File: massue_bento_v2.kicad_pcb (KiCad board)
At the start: 2 copper layers, 100 x 21 mm, 69 parts, among them K1 CONN_3, K2 CONN_3, K3 CONN_3, P1 TST, P10 CONN_1, P11 TST, P12 TST, P13 TST, P14 TST, P15 TST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

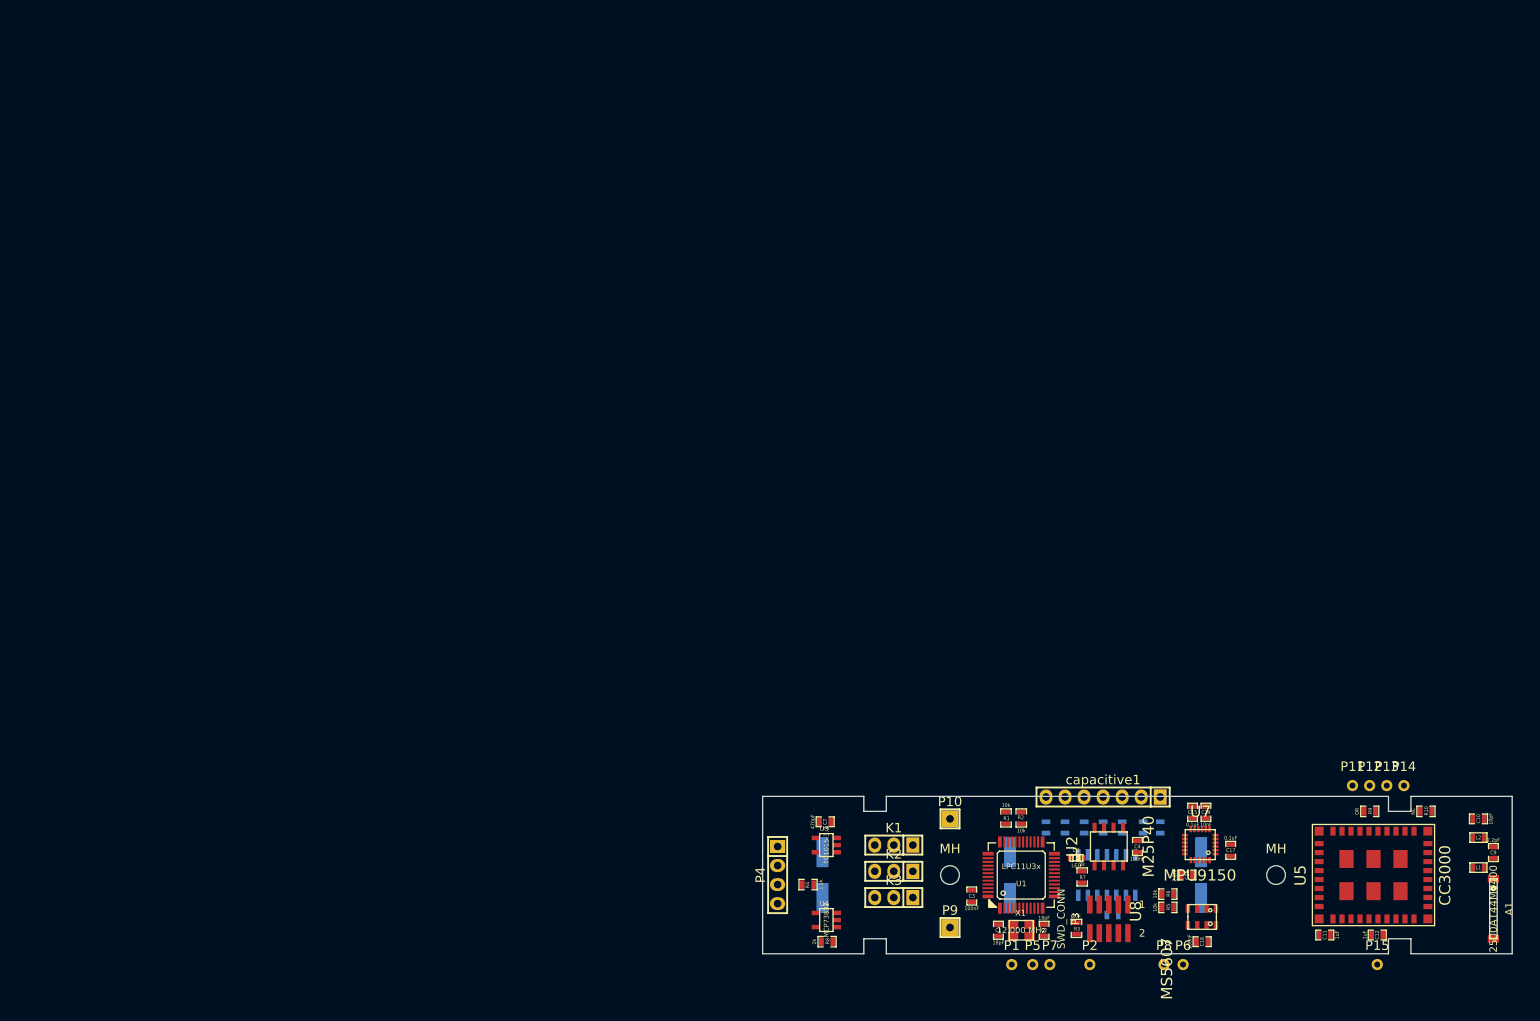
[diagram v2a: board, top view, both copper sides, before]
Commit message: Begin RF routing
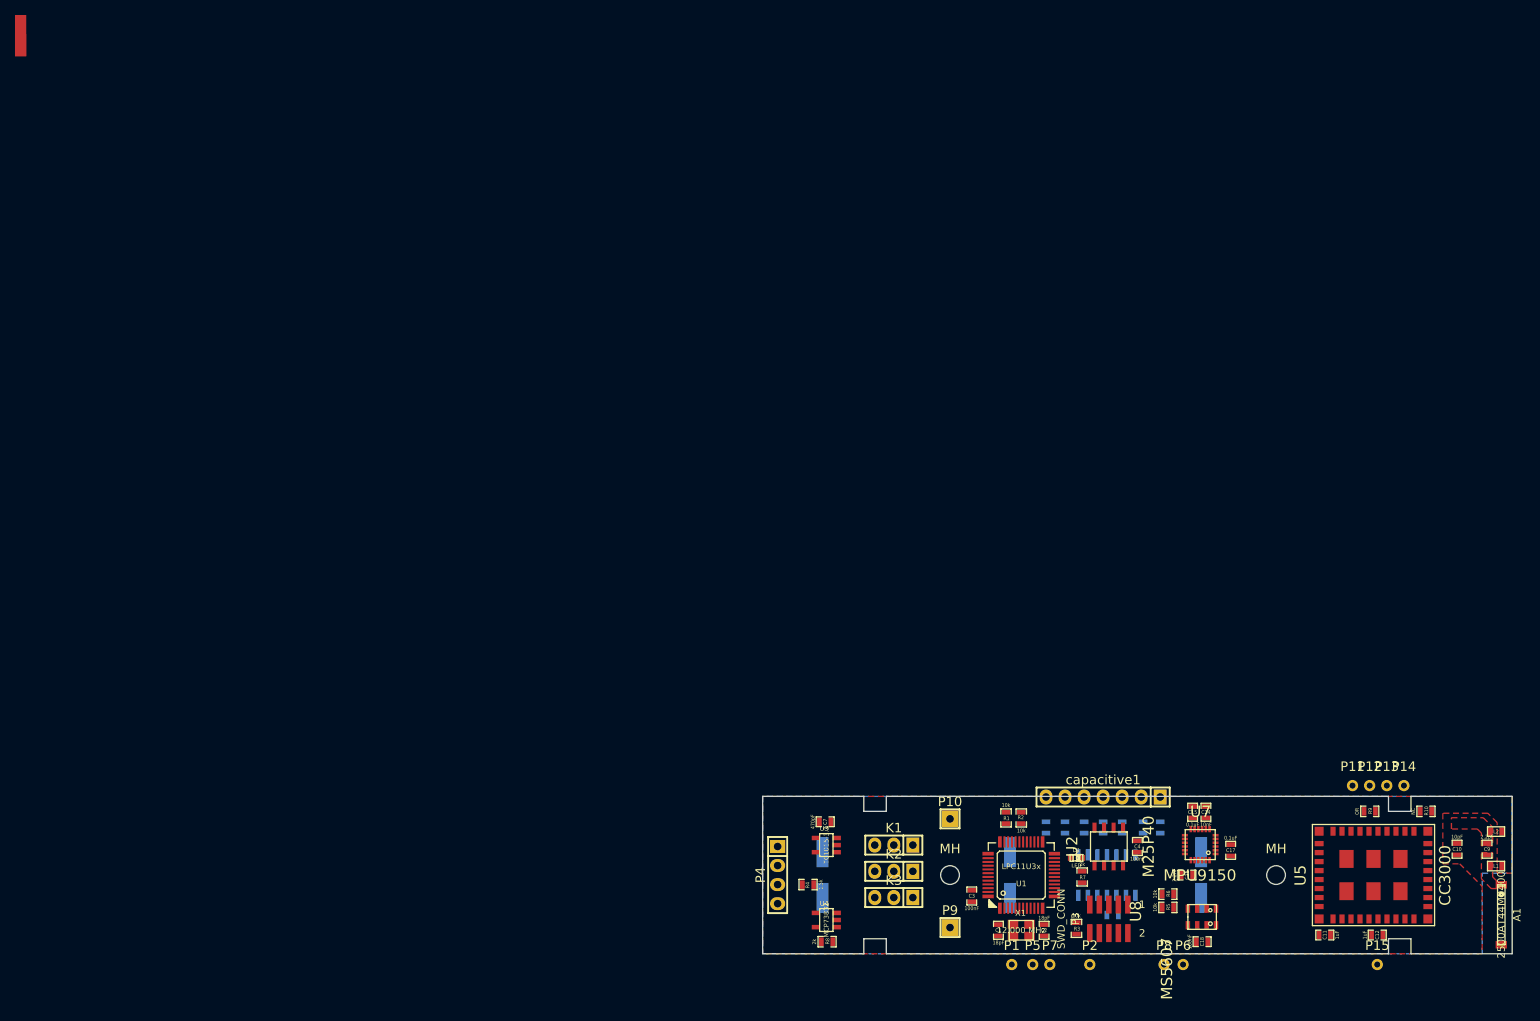
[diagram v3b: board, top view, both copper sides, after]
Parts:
- added GAP: VAL**, GAP, F.Cu at (0.00, 0.00)
- added STUB (x2): VAL**, STUB, F.Cu at (0.00, 0.00)
- moved C10 4.95 mm to (191.7, 106.5), turned to 270 degrees
- moved L2 2.48 mm to (196.8, 104.2), turned to 0 degrees
- moved L1 2.36 mm to (196.8, 108.8), turned to 0 degrees
- moved A1 1.32 mm to (197.6, 115.3)
- moved C9 0.96 mm to (195.7, 106.5)
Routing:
- added copper zone on B.Cu, net GND
- added copper zone on F.Cu, net GND
- added copper zone on F.Cu, net Net-(A1-Pad1)
- added copper zone on F.Cu, net Net-(C10-Pad1)
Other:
- board text added: "Antenna layout #2 from 2500AT44M0400 datasheet"
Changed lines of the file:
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@@
   (general
     (links 188)
-    (no_connects 188)
-    (area 96.979115 93.798 202.917858 125.8972)
+    (no_connects 121)
+    (area -0.95 -4.95 223.944051 125.8972)
     (thickness 1.6)
-    (drawings 20)
+    (drawings 21)
     (tracks 0)
     (zones 0)
-    (modules 69)
+    (modules 72)
     (nets 67)
   )
@@
   )
   (setup
-    (last_trace_width 0.8)
+    (last_trace_width 1.5)
     (user_trace_width 0.25)
     (user_trace_width 0.4)
     (user_trace_width 0.8)
+    (user_trace_width 1)
+    (user_trace_width 1.2)
     (user_trace_width 1.5)
     (trace_clearance 0.2)
-    (zone_clearance 0.508)
-    (zone_45_only no)
+    (zone_clearance 0.4)
+    (zone_45_only yes)
     (trace_min 0.1524)
     (segment_width 0.2)
@@
     (add_net VBAT)
   )
+  (module STUB (layer F.Cu)
+    (at 0 0)
+    (fp_text reference STUB (at 0 0.00003) (layer F.SilkS)
+      (effects (font (size 0.00003 0.00003) (thickness 0.000007)))
+    )
+    (fp_text value VAL** (at 0 -0.00003) (layer F.SilkS)
+      (effects (font (size 0.00003 0.00003) (thickness 0.000007)))
+    )
+    (pad 1 smd rect (at 0 0) (size 1.5 1.5) (layers F.Cu))
+    (pad 1 smd rect (at 0 -2.75) (size 1.5 4) (layers F.Cu))
+  )
+  (module GAP (layer F.Cu)
+    (at 0 0)
+    (fp_text reference GAP (at 0 0.00003) (layer F.SilkS)
+      (effects (font (size 0.00003 0.00003) (thickness 0.000007)))
+    )
+    (fp_text value VAL** (at 0 -0.00003) (layer F.SilkS)
+      (effects (font (size 0.00003 0.00003) (thickness 0.000007)))
+    )
+    (pad 2 smd rect (at -0.2 0) (size 0.2 0.2) (layers F.Cu))
+    (pad 1 smd rect (at 0.2 0) (size 0.2 0.2) (layers F.Cu))
+  )
+  (module STUB (layer F.Cu)
+    (at 0 0)
+    (fp_text reference STUB (at 0 0.00003) (layer F.SilkS)
+      (effects (font (size 0.00003 0.00003) (thickness 0.000007)))
+    )
+    (fp_text value VAL** (at 0 -0.00003) (layer F.SilkS)
+      (effects (font (size 0.00003 0.00003) (thickness 0.000007)))
+    )
+    (pad 1 smd rect (at 0 0) (size 1.5 1.5) (layers F.Cu))
+    (pad 1 smd rect (at 0 -1.5) (size 1.5 1.5) (layers F.Cu))
+  )
   (module Tom:2500AT44M0400 (layer F.Cu)
-    (at 196.5 114.5 90)
+    (at 197.55 115.3 90)
     (descr "Johanson 2.4GHz wideband chip antenna")
     (tags antenna;ANT)
@@
   )
   (module SMD_Packages:SM0603_Capa (layer F.Cu)
-    (at 196.5 107 270)
+    (at 195.65 106.55 270)
     (attr smd)
     (fp_text reference C9 (at 0 0 360) (layer F.SilkS)
@@
   )
   (module SMD_Packages:SM0603_Capa (layer F.Cu)
-    (at 194.5 102.5 180)
-    (attr smd)
-    (fp_text reference C10 (at 0 0 270) (layer F.SilkS)
-      (effects (font (size 0.508 0.4572) (thickness 0.1143)))
-    )
-    (fp_text value 10pF (at -1.651 0 270) (layer F.SilkS)
+    (at 191.65 106.55 270)
+    (attr smd)
+    (fp_text reference C10 (at 0 0 360) (layer F.SilkS)
+      (effects (font (size 0.508 0.4572) (thickness 0.1143)))
+    )
+    (fp_text value 10pF (at -1.651 0 360) (layer F.SilkS)
       (effects (font (size 0.508 0.4572) (thickness 0.1143)))
     )
@@
     (fp_line (start 1.19888 -0.635) (end 1.19888 0.635) (layer F.SilkS) (width 0.11938))
     (fp_line (start -1.19888 0.635) (end -1.19888 -0.635) (layer F.SilkS) (width 0.11938))
-    (pad 1 smd rect (at -0.762 0 180) (size 0.635 1.143) (layers F.Cu F.Paste F.Mask)
+    (pad 1 smd rect (at -0.762 0 270) (size 0.635 1.143) (layers F.Cu F.Paste F.Mask)
       (net 9 "Net-(C10-Pad1)"))
-    (pad 2 smd rect (at 0.762 0 180) (size 0.635 1.143) (layers F.Cu F.Paste F.Mask)
+    (pad 2 smd rect (at 0.762 0 270) (size 0.635 1.143) (layers F.Cu F.Paste F.Mask)
       (net 10 "Net-(C10-Pad2)"))
     (model smd\capacitors\C0603.wrl
@@
   )
   (module SMD_Packages:SM0603 (layer F.Cu)
-    (at 194.5 109 180)
-    (attr smd)
-    (fp_text reference L1 (at 0 0 180) (layer F.SilkS)
-      (effects (font (size 0.508 0.4572) (thickness 0.1143)))
-    )
-    (fp_text value NC (at 0 0 180) (layer F.SilkS) hide
+    (at 196.85 108.8)
+    (attr smd)
+    (fp_text reference L1 (at 0 0) (layer F.SilkS)
+      (effects (font (size 0.508 0.4572) (thickness 0.1143)))
+    )
+    (fp_text value NC (at 0 0) (layer F.SilkS) hide
       (effects (font (size 0.508 0.4572) (thickness 0.1143)))
     )
@@
     (fp_line (start 1.143 0.635) (end -1.143 0.635) (layer F.SilkS) (width 0.127))
     (fp_line (start -1.143 0.635) (end -1.143 -0.635) (layer F.SilkS) (width 0.127))
-    (pad 1 smd rect (at -0.762 0 180) (size 0.635 1.143) (layers F.Cu F.Paste F.Mask)
+    (pad 1 smd rect (at -0.762 0) (size 0.635 1.143) (layers F.Cu F.Paste F.Mask)
       (net 1 "Net-(A1-Pad1)"))
-    (pad 2 smd rect (at 0.762 0 180) (size 0.635 1.143) (layers F.Cu F.Paste F.Mask)
+    (pad 2 smd rect (at 0.762 0) (size 0.635 1.143) (layers F.Cu F.Paste F.Mask)
       (net 3 GND))
     (model smd\resistors\R0603.wrl
@@
   )
   (module SMD_Packages:SM0603 (layer F.Cu)
-    (at 194.5 105 180)
-    (attr smd)
-    (fp_text reference L2 (at 0 0 180) (layer F.SilkS)
-      (effects (font (size 0.508 0.4572) (thickness 0.1143)))
-    )
-    (fp_text value 2.2nH (at 0 0 180) (layer F.SilkS) hide
+    (at 196.85 104.2)
+    (attr smd)
+    (fp_text reference L2 (at 0 0) (layer F.SilkS)
+      (effects (font (size 0.508 0.4572) (thickness 0.1143)))
+    )
+    (fp_text value 2.2nH (at 0 0) (layer F.SilkS) hide
       (effects (font (size 0.508 0.4572) (thickness 0.1143)))
     )
@@
     (fp_line (start 1.143 0.635) (end -1.143 0.635) (layer F.SilkS) (width 0.127))
     (fp_line (start -1.143 0.635) (end -1.143 -0.635) (layer F.SilkS) (width 0.127))
-    (pad 1 smd rect (at -0.762 0 180) (size 0.635 1.143) (layers F.Cu F.Paste F.Mask)
+    (pad 1 smd rect (at -0.762 0) (size 0.635 1.143) (layers F.Cu F.Paste F.Mask)
       (net 9 "Net-(C10-Pad1)"))
-    (pad 2 smd rect (at 0.762 0 180) (size 0.635 1.143) (layers F.Cu F.Paste F.Mask)
+    (pad 2 smd rect (at 0.762 0) (size 0.635 1.143) (layers F.Cu F.Paste F.Mask)
       (net 3 GND))
     (model smd\resistors\R0603.wrl
@@
       (net 39 "Net-(P15-Pad1)"))
   )
+  (gr_text "Antenna layout #2 from 2500AT44M0400 datasheet" (at 204.25 122) (layer Cmts.User)
+    (effects (font (size 1 1) (thickness 0.15)))
+  )
   (gr_line (start 185.5 120.5) (end 199 120.5) (angle 90) (layer Edge.Cuts) (width 0.15))
   (gr_line (start 185.5 118.5) (end 185.5 120.5) (angle 90) (layer Edge.Cuts) (width 0.15))
@@
   (gr_line (start 199 120.5) (end 199 99.5) (angle 90) (layer Edge.Cuts) (width 0.15))
   (gr_line (start 99 99.5) (end 99 120.5) (angle 90) (layer Edge.Cuts) (width 0.15))
+  (zone (net 0) (net_name "") (layer F.Cu) (hatch edge 0.508)
+    (connect_pads (clearance 0.16))
+    (min_thickness 0.16)
+    (keepout (tracks not_allowed) (vias not_allowed) (copperpour allowed))
+    (fill (arc_segments 16) (thermal_gap 0.16) (thermal_bridge_width 0.35))
+    (polygon
+      (pts
+        (xy 199 120.5) (xy 195 120.5) (xy 195 109.8) (xy 199 109.8)
+      )
+    )
+  )
+  (zone (net 0) (net_name "") (layer B.Cu) (hatch edge 0.508)
+    (connect_pads (clearance 0.16))
+    (min_thickness 0.16)
+    (keepout (tracks not_allowed) (vias not_allowed) (copperpour allowed))
+    (fill (arc_segments 16) (thermal_gap 0.16) (thermal_bridge_width 0.35))
+    (polygon
+      (pts
+        (xy 199 120.5) (xy 195 120.5) (xy 195 109.8) (xy 199 109.8)
+      )
+    )
+  )
+  (zone (net 9) (net_name "Net-(C10-Pad1)") (layer F.Cu) (hatch edge 0.508)
+    (connect_pads yes (clearance 0))
+    (min_thickness 0.16)
+    (fill yes (arc_segments 16) (thermal_gap 0.16) (thermal_bridge_width 0.35) (smoothing fillet) (radius 0.2))
+    (polygon
+      (pts
+        (xy 196.4 106.1) (xy 194.9 106.1) (xy 194.9 104.4) (xy 194.35 103.85) (xy 190.9 103.85)
+        (xy 190.9 102.35) (xy 195.15 102.35) (xy 196.4 103.6)
+      )
+    )
+  )
+  (zone (net 1) (net_name "Net-(A1-Pad1)") (layer F.Cu) (hatch edge 0.508)
+    (connect_pads yes (clearance 0))
+    (min_thickness 0.16)
+    (fill yes (arc_segments 16) (thermal_gap 0.16) (thermal_bridge_width 0.35) (smoothing fillet) (radius 0.2))
+    (polygon
+      (pts
+        (xy 196.95 111.8) (xy 196.2 111.8) (xy 194.9 110.5) (xy 194.9 107) (xy 196.4 107)
+        (xy 196.4 110.25) (xy 196.95 110.8)
+      )
+    )
+  )
+  (zone (net 3) (net_name GND) (layer F.Cu) (hatch edge 0.508)
+    (connect_pads (clearance 0.4))
+    (min_thickness 0.3)
+    (fill yes (arc_segments 16) (thermal_gap 0.16) (thermal_bridge_width 0.35))
+    (polygon
+      (pts
+        (xy 199 109.75) (xy 197 109.75) (xy 197 103) (xy 195.75 101.75) (xy 189.75 101.75)
+        (xy 189.75 108.5) (xy 192 108.5) (xy 195 111.5) (xy 195 120.5) (xy 99 120.5)
+        (xy 99 99.5) (xy 199 99.5)
+      )
+    )
+  )
+  (zone (net 3) (net_name GND) (layer B.Cu) (hatch edge 0.508)
+    (connect_pads (clearance 0.4))
+    (min_thickness 0.3)
+    (fill yes (arc_segments 16) (thermal_gap 0.16) (thermal_bridge_width 0.35))
+    (polygon
+      (pts
+        (xy 99 120.5) (xy 195 120.5) (xy 195 109.75) (xy 199 109.75) (xy 199 99.5)
+        (xy 99 99.5)
+      )
+    )
+  )
 )

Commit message: CC3000 and RF routing
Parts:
- removed GAP: VAL**, GAP
- removed STUB (x2): VAL**, STUB
- P1, P11, P15, P2, P5, P6, P7, P8: footprint Measurement_Points:Measurement_Point_Round-TH_Small -> Measurement_Points:Measurement_Point_Round-SMD-Pad_Small
- P12, P13, P14: footprint Measurement_Points:Measurement_Point_Round-TH_Small -> Measurement_Points:Measurement_Point_Round-SMD-Pad_Small; moved to B.Cu
- moved R10 4.34 mm to (183.2, 101.5)
- moved P15 3.26 mm to (182.1, 118.9)
- moved L2 3.23 mm to (193.7, 103.8), turned to 90 degrees
- moved P11 3.06 mm to (177.4, 101.1)
- moved P14 3.05 mm to (184.7, 101.1)
- moved P12 3.05 mm to (180.0, 101.1)
- moved P13 3.05 mm to (182.3, 101.1)
- moved C12 1.90 mm to (179.1, 118.0), turned to 180 degrees
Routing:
- net GND: track 0.00 -> 98.4 mm, vias 0 -> 56
- net /RF/WL_EN2: track 0.00 -> 4.86 mm
- net Net-(C10-Pad2): track 0.00 -> 4.03 mm
- net Net-(P15-Pad1): track 0.00 -> 3.47 mm
- net Net-(P12-Pad1): track 0.00 -> 3.08 mm, vias 0 -> 1
- net Net-(P11-Pad1): track 0.00 -> 3.06 mm
- net Net-(P13-Pad1): track 0.00 -> 3.05 mm, vias 0 -> 1
- net Net-(P14-Pad1): track 0.00 -> 3.05 mm, vias 0 -> 1
- net Net-(U5-Pad28): track 0.00 -> 2.97 mm
- net /RF/WL_EN1: track 0.00 -> 2.88 mm
- net VBAT: track 0.00 -> 2.29 mm
- net +3.3V: track 0.00 -> 2.17 mm
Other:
- outline, holes or cut-outs redrawn

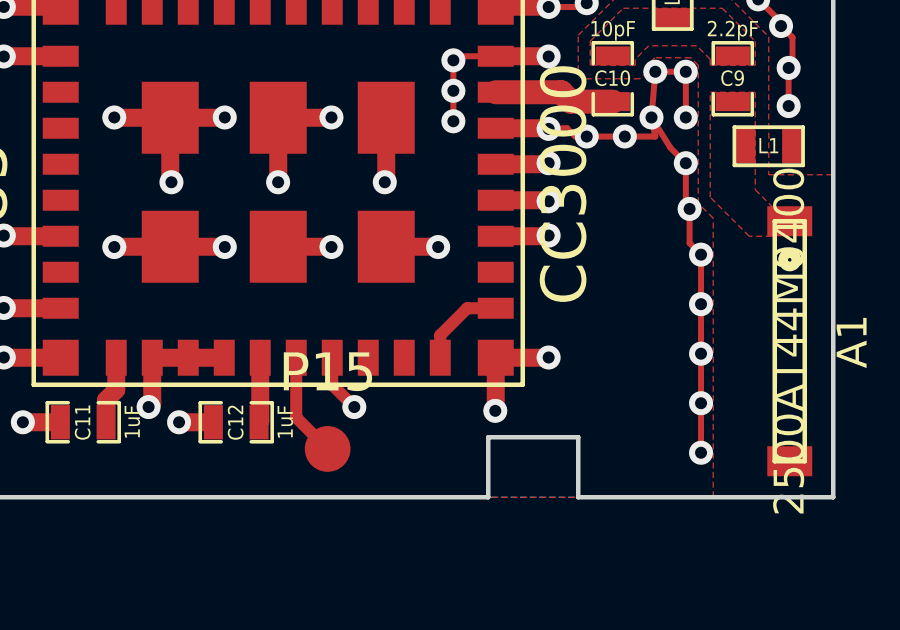
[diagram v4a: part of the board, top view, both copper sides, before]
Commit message: Fix: error in CC3000 component pinout
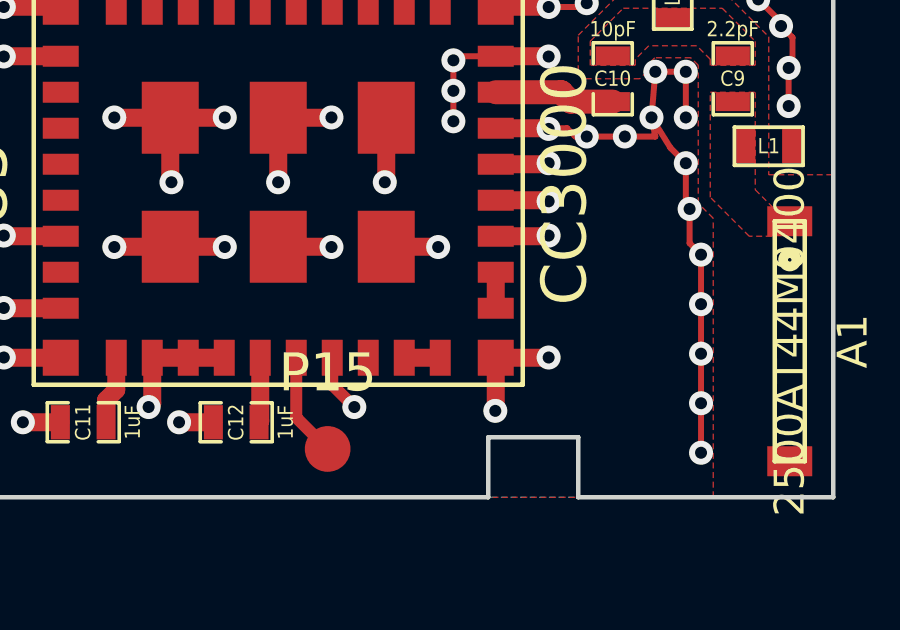
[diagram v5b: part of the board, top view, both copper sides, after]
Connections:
- U5 pad 27: (no net) -> Net-(U5-Pad27)
- U5 pad 28: Net-(U5-Pad28) -> Net-(U5-Pad27)
- U5 pad 29: Net-(U5-Pad28) -> Net-(U5-Pad29)
- U5 pad 30: (no net) -> Net-(U5-Pad29)
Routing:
- net Net-(U5-Pad28): track 2.97 -> 0.00 mm
- net Net-(U5-Pad27): track 0.00 -> 1.20 mm
- net Net-(U5-Pad29): track 0.00 -> 1.20 mm
